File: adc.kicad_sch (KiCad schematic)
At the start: 37 parts, among them J5 Conn_01x03_Pin, J8 Conn_01x03_Pin, U21 LTC2299xUP

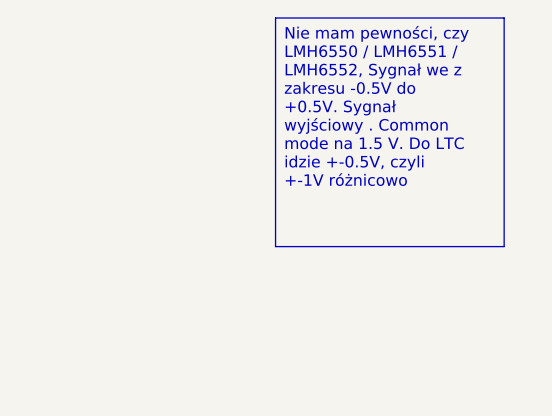
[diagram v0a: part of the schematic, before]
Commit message: Remove the stage between DAC and FET buffer
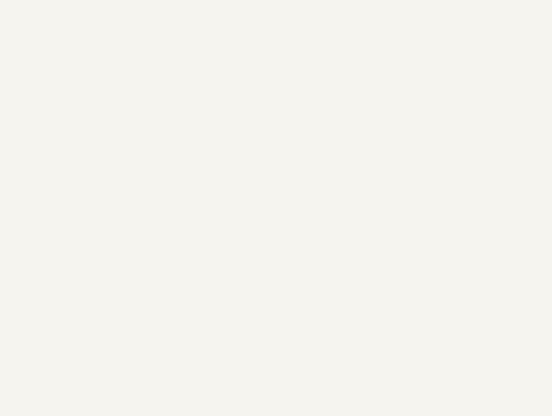
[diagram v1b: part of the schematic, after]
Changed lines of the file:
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@@
-		)
-	)
-	(text_box "Nie mam pewności, czy LMH6550 / LMH6551 / LMH6552, Sygnał we z zakresu -0.5V do +0.5V. Sygnał wyjściowy . Common mode na 1.5 V. Do LTC idzie +-0.5V, czyli +-1V różnicowo"
-		(exclude_from_sim no)
-		(at 372.11 24.13 0)
-		(size 25.4 25.4)
-		(margins 0.9525 0.9525 0.9525 0.9525)
-		(stroke
-			(width 0)
-			(type solid)
-		)
-		(fill
-			(type none)
-		)
-		(effects
-			(font
-				(size 1.27 1.27)
-			)
-			(justify left top)
 		)
 	)

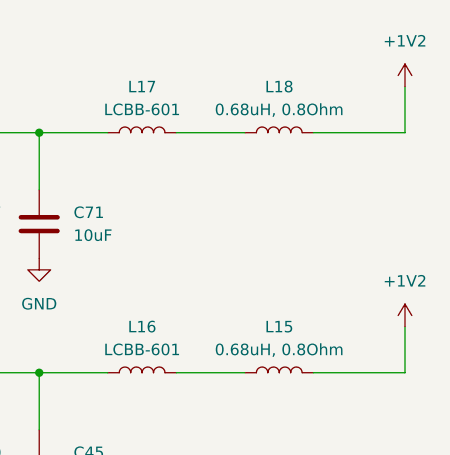
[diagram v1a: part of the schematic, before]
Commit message: Finished up schematic? - Added missing PSU lines
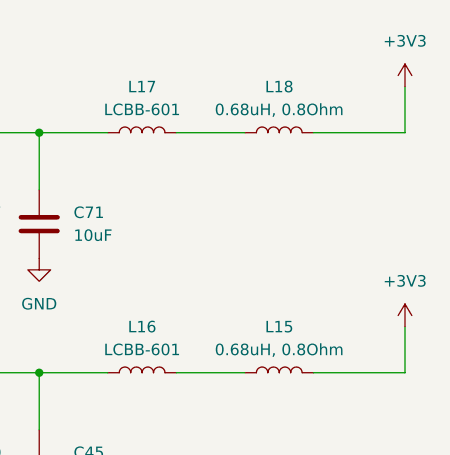
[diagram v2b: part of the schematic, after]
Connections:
- net +1V2 is gone; now on net +3V3: L15.1, L18.1
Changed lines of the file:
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@@
 	(wire
 		(pts
+			(xy 312.42 83.82) (xy 312.42 78.74)
+		)
+		(stroke
+			(width 0)
+			(type default)
+		)
+	)
+	(wire
+		(pts
 			(xy 237.49 57.15) (xy 237.49 130.81)
 		)
@@
 	(wire
 		(pts
-			(xy 312.42 83.82) (xy 312.42 78.74)
-		)
-		(stroke
-			(width 0)
-			(type default)
-		)
-	)
-	(wire
-		(pts
 			(xy 232.41 227.33) (xy 232.41 231.14)
 		)
@@
 	)
 	(symbol
-		(lib_id "power:+3V3")
-		(at 312.42 78.74 0)
-		(unit 1)
-		(exclude_from_sim no)
-		(in_bom yes)
-		(on_board yes)
-		(dnp no)
-		(fields_autoplaced yes)
-		(property "Reference" "#PWR0142"
-			(at 312.42 82.55 0)
-			(effects
-				(font
-					(size 1.27 1.27)
-				)
-				(hide yes)
-			)
-		)
-		(property "Value" "+1V2"
-			(at 312.42 73.66 0)
-			(effects
-				(font
-					(size 1.27 1.27)
-				)
-			)
-		)
-		(property "Footprint" ""
-			(at 312.42 78.74 0)
-			(effects
-				(font
-					(size 1.27 1.27)
-				)
-				(hide yes)
-			)
-		)
-		(property "Datasheet" ""
-			(at 312.42 78.74 0)
-			(effects
-				(font
-					(size 1.27 1.27)
-				)
-				(hide yes)
-			)
-		)
-		(property "Description" "Power symbol creates a global label with name \"+3V3\""
-			(at 312.42 78.74 0)
-			(effects
-				(font
-					(size 1.27 1.27)
-				)
-				(hide yes)
-			)
-		)
-		(pin "1"
-		)
-		(instances
-			(project "DigitalOsciloscope"
-				(path "/553deb7b-4100-40fe-99d2-0c7b4b56aad2/800cc051-5da0-4b0f-90b7-cfba3f489ea8"
-					(reference "#PWR0142")
-					(unit 1)
-				)
-			)
-		)
-	)
-	(symbol
 		(lib_id "Device:L")
 		(at 128.27 57.15 90)
@@
 	)
 	(symbol
-		(lib_id "power:+3V3")
-		(at 312.42 52.07 0)
-		(unit 1)
-		(exclude_from_sim no)
-		(in_bom yes)
-		(on_board yes)
-		(dnp no)
-		(fields_autoplaced yes)
-		(property "Reference" "#PWR0106"
-			(at 312.42 55.88 0)
-			(effects
-				(font
-					(size 1.27 1.27)
-				)
-				(hide yes)
-			)
-		)
-		(property "Value" "+1V2"
-			(at 312.42 46.99 0)
-			(effects
-				(font
-					(size 1.27 1.27)
-				)
-			)
-		)
-		(property "Footprint" ""
-			(at 312.42 52.07 0)
-			(effects
-				(font
-					(size 1.27 1.27)
-				)
-				(hide yes)
-			)
-		)
-		(property "Datasheet" ""
-			(at 312.42 52.07 0)
-			(effects
-				(font
-					(size 1.27 1.27)
-				)
-				(hide yes)
-			)
-		)
-		(property "Description" "Power symbol creates a global label with name \"+3V3\""
-			(at 312.42 52.07 0)
-			(effects
-				(font
-					(size 1.27 1.27)
-				)
-				(hide yes)
-			)
-		)
-		(pin "1"
-		)
-		(instances
-			(project "DigitalOsciloscope"
-				(path "/553deb7b-4100-40fe-99d2-0c7b4b56aad2/800cc051-5da0-4b0f-90b7-cfba3f489ea8"
-					(reference "#PWR0106")
-					(unit 1)
-				)
-			)
-		)
-	)
-	(symbol
 		(lib_id "Device:L")
 		(at 143.51 57.15 90)
@@
 	)
 	(symbol
+		(lib_id "power:+3V3")
+		(at 312.42 52.07 0)
+		(unit 1)
+		(exclude_from_sim no)
+		(in_bom yes)
+		(on_board yes)
+		(dnp no)
+		(fields_autoplaced yes)
+		(property "Reference" "#PWR0272"
+			(at 312.42 55.88 0)
+			(effects
+				(font
+					(size 1.27 1.27)
+				)
+				(hide yes)
+			)
+		)
+		(property "Value" "+3V3"
+			(at 312.42 46.99 0)
+			(effects
+				(font
+					(size 1.27 1.27)
+				)
+			)
+		)
+		(property "Footprint" ""
+			(at 312.42 52.07 0)
+			(effects
+				(font
+					(size 1.27 1.27)
+				)
+				(hide yes)
+			)
+		)
+		(property "Datasheet" ""
+			(at 312.42 52.07 0)
+			(effects
+				(font
+					(size 1.27 1.27)
+				)
+				(hide yes)
+			)
+		)
+		(property "Description" "Power symbol creates a global label with name \"+3V3\""
+			(at 312.42 52.07 0)
+			(effects
+				(font
+					(size 1.27 1.27)
+				)
+				(hide yes)
+			)
+		)
+		(pin "1"
+		)
+		(instances
+			(project "DigitalOsciloscope"
+				(path "/553deb7b-4100-40fe-99d2-0c7b4b56aad2/800cc051-5da0-4b0f-90b7-cfba3f489ea8"
+					(reference "#PWR0272")
+					(unit 1)
+				)
+			)
+		)
+	)
+	(symbol
 		(lib_id "Device:C")
 		(at 173.99 90.17 0)
@@
 					(unit 1)
 				)
+			)
+		)
+	)
+	(symbol
+		(lib_id "power:+3V3")
+		(at 312.42 78.74 0)
+		(unit 1)
+		(exclude_from_sim no)
+		(in_bom yes)
+		(on_board yes)
+		(dnp no)
+		(fields_autoplaced yes)
+		(property "Reference" "#PWR0106"
+			(at 312.42 82.55 0)
+			(effects
+				(font
+					(size 1.27 1.27)
+				)
+				(hide yes)
+			)
+		)
+		(property "Value" "+3V3"
+			(at 312.42 73.66 0)
+			(effects
+				(font
+					(size 1.27 1.27)
+				)
+			)
+		)
+		(property "Footprint" ""
+			(at 312.42 78.74 0)
+			(effects
+				(font
+					(size 1.27 1.27)
+				)
+				(hide yes)
+			)
+		)
+		(property "Datasheet" ""
+			(at 312.42 78.74 0)
+			(effects
+				(font
+					(size 1.27 1.27)
+				)
+				(hide yes)
+			)
+		)
+		(property "Description" "Power symbol creates a global label with name \"+3V3\""
+			(at 312.42 78.74 0)
+			(effects
+				(font
+					(size 1.27 1.27)
+				)
+				(hide yes)
+			)
+		)
+		(pin "1"
+		)
+		(instances
+			(project "DigitalOsciloscope"
+				(path "/553deb7b-4100-40fe-99d2-0c7b4b56aad2/800cc051-5da0-4b0f-90b7-cfba3f489ea8"
+					(reference "#PWR0106")
+					(unit 1)
+				)

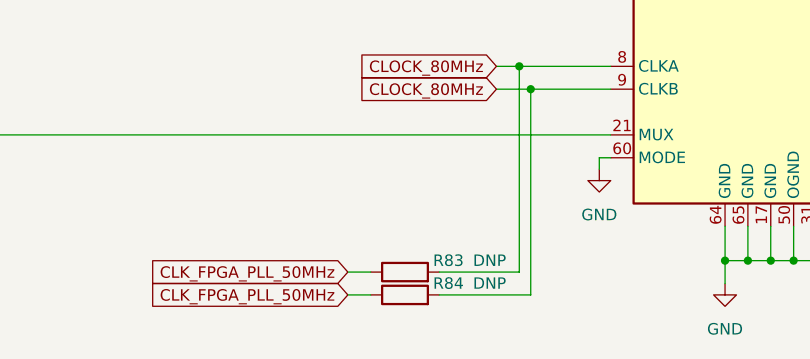
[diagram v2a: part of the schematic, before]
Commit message: Start working on ERC, properly annotate DNP elements
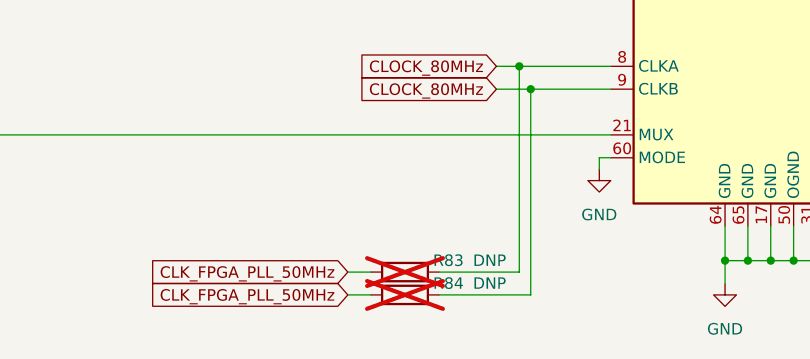
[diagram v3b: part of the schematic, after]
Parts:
- R83, R84: now not fitted
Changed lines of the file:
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@@
 		(in_bom yes)
 		(on_board yes)
-		(dnp no)
+		(dnp yes)
 		(property "Reference" "R84"
 			(at 196.596 233.68 90)
@@
 		(in_bom yes)
 		(on_board yes)
-		(dnp no)
+		(dnp yes)
 		(property "Reference" "R83"
 			(at 196.596 231.14 90)

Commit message: Fix ERC
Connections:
- net OVERFLOW: now reaches U21.57 (OFA)

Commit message: Add all footprints
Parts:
- J4: renamed from J8; footprint (none) -> TerminalBlock:TerminalBlock_MaiXu_MX126-5.0-03P_1x03_P5.00mm
- J5: footprint (none) -> TerminalBlock:TerminalBlock_MaiXu_MX126-5.0-03P_1x03_P5.00mm
- L33: renamed from L13; footprint (none) -> Inductor_SMD:L_0805_2012Metric
- L34: renamed from L7; footprint (none) -> Inductor_SMD:L_0805_2012Metric
- L35: renamed from L14; footprint (none) -> Inductor_SMD:L_0805_2012Metric
- L36: renamed from L8; footprint (none) -> Inductor_SMD:L_0805_2012Metric
- L37: renamed from L17; footprint (none) -> Inductor_SMD:L_0805_2012Metric
- L38: renamed from L16; footprint (none) -> Inductor_SMD:L_0805_2012Metric
- L39: renamed from L18; footprint (none) -> Inductor_SMD:L_0805_2012Metric
- L40: renamed from L15; footprint (none) -> Inductor_SMD:L_0805_2012Metric
- renumbered C39 to C76, C33 to C77, C40 to C78, C34 to C79, C41 to C80, C35 to C81, C16 to C82, C15 to C83, C42 to C84, C36 to C85, C18 to C86, C54 to C87, C43 to C88, C37 to C89, C17 to C90, C55 to C91, C44 to C92, C38 to C93, C46 to C94, C19 to C95, C47 to C96, C20 to C97, C71 to C98, C45 to C99, R83 to R56, R84 to R57, U21 to U9
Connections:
- net GND: no longer U9.11 (REFLB), U9.12 (REFLB), U9.13 (REFHB), U9.14 (REFHB)
- new net: U9.11 (REFLB), U9.12 (REFLB)
- new net: U9.13 (REFHB), U9.14 (REFHB)

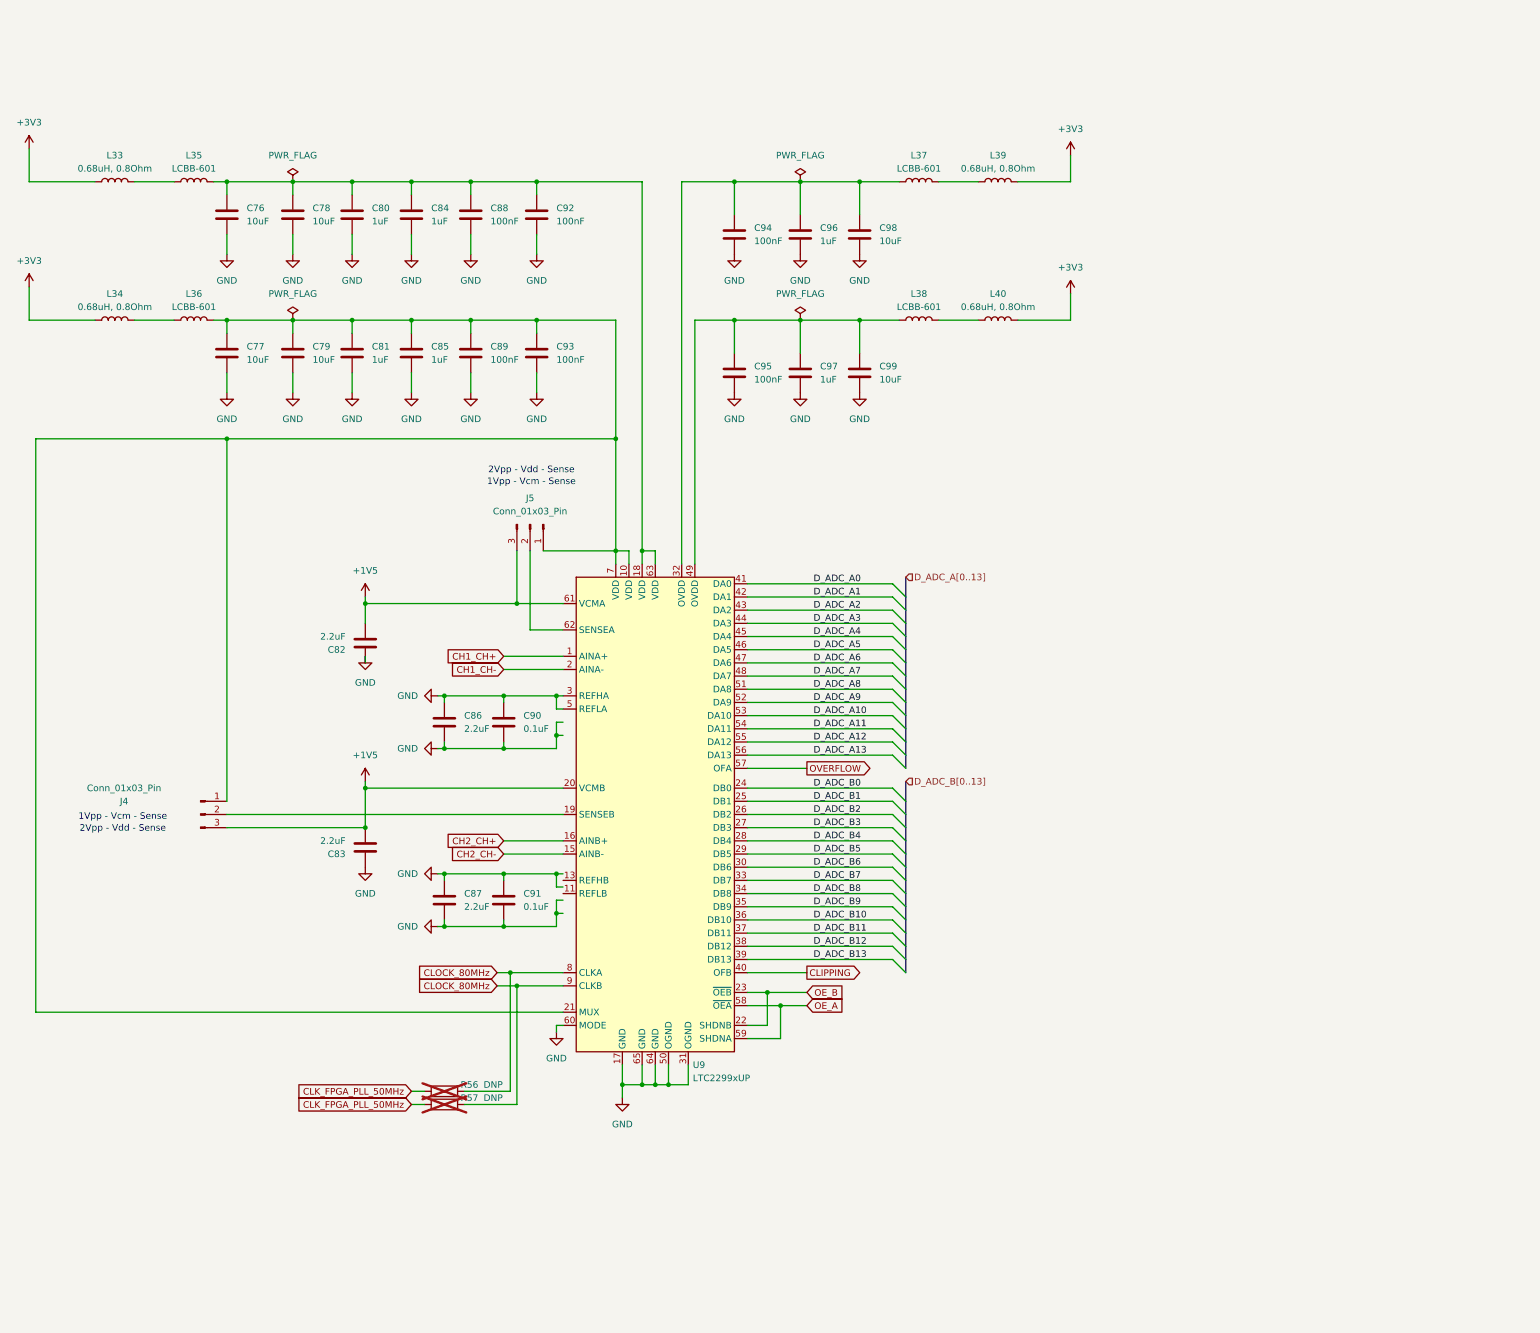
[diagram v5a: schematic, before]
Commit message: Apply changes after review, left to fix: comparator histeresis, PSU missing lines?
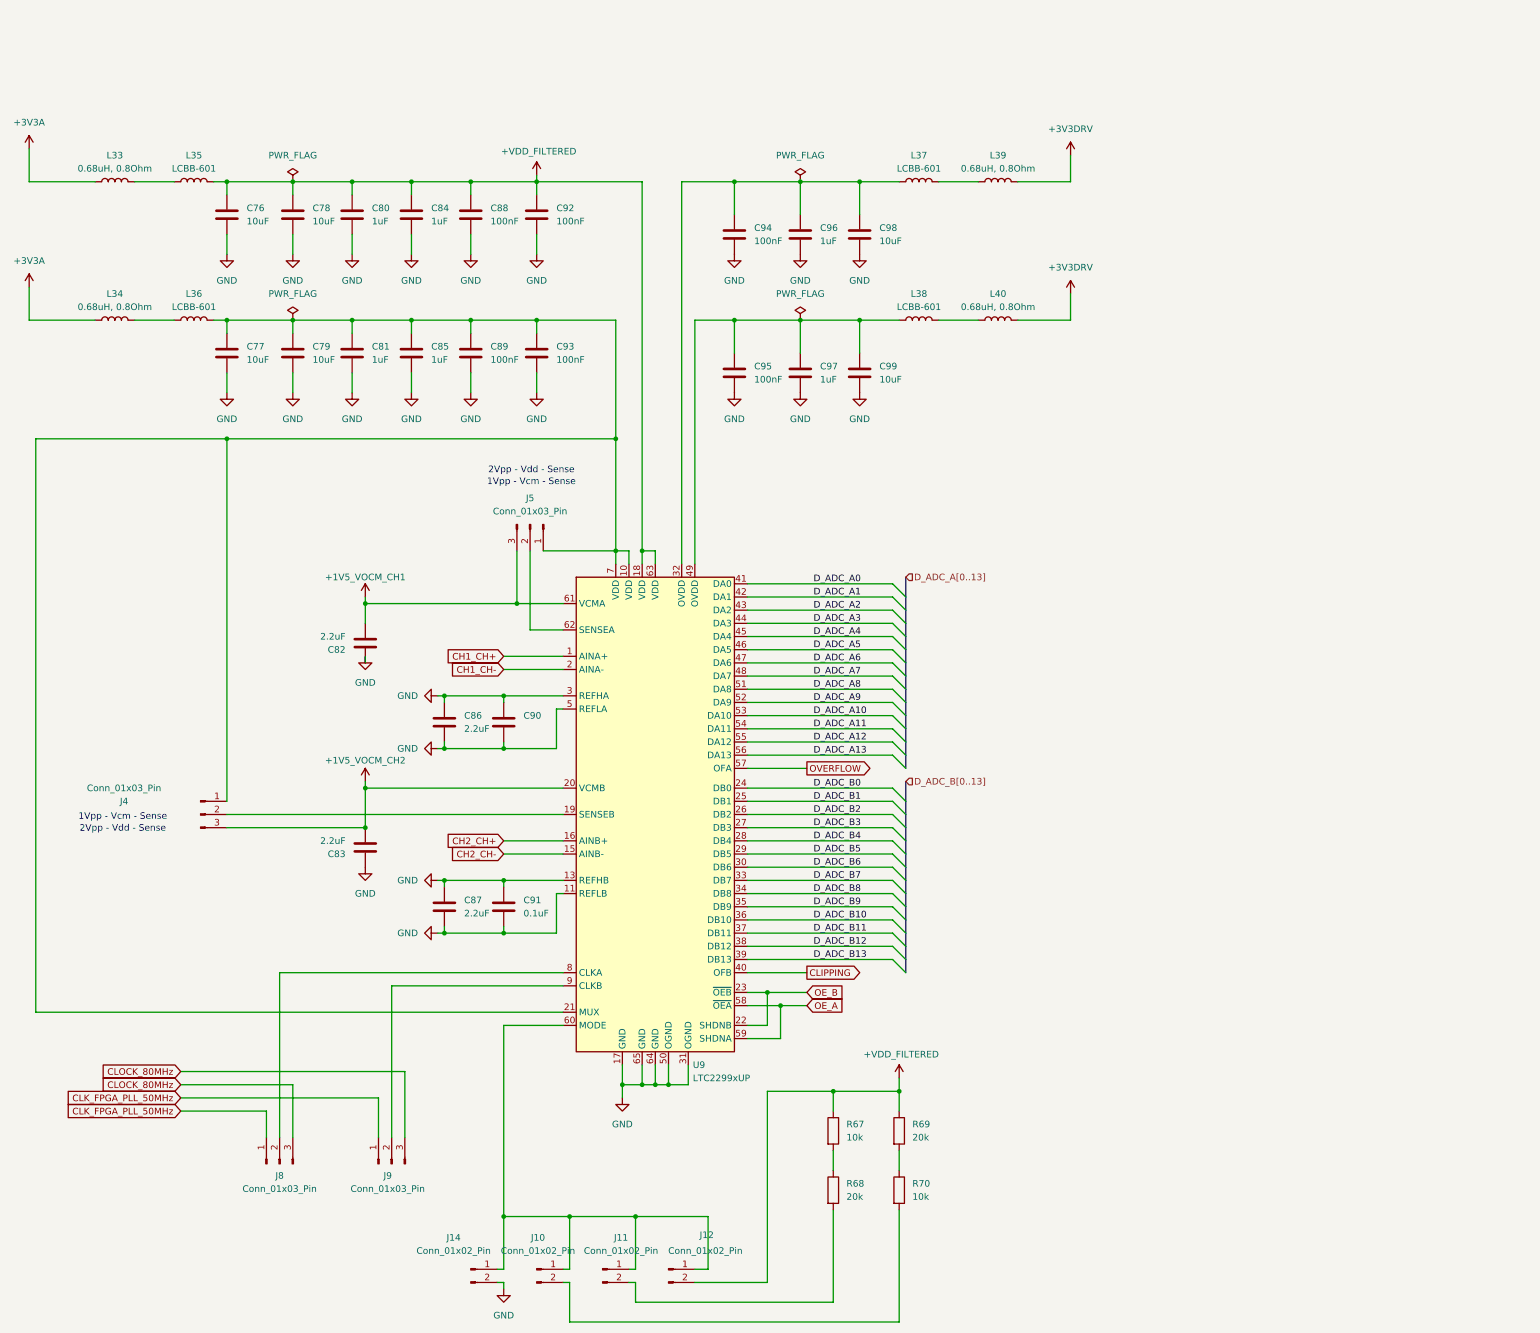
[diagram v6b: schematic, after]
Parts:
- removed R56, R57: DNP, Resistor_SMD:R_0805_2012Metric, symbol Device:R
- added J10, J11, J12, J14: Conn_01x02_Pin, TerminalBlock:TerminalBlock_MaiXu_MX126-5.0-02P_1x02_P5.00mm, symbol Connector:Conn_01x02_Pin
- added J8, J9: Conn_01x03_Pin, TerminalBlock:TerminalBlock_MaiXu_MX126-5.0-03P_1x03_P5.00mm, symbol Connector:Conn_01x03_Pin
- added R67, R70: 10k, Resistor_SMD:R_0805_2012Metric, symbol Device:R
- added R68, R69: 20k, Resistor_SMD:R_0805_2012Metric, symbol Device:R
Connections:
- net CLK_FPGA_PLL_50MHz: now also J8.1 (Pin_1), J9.1 (Pin_1)
- net CLOCK_80MHz: now also J8.3 (Pin_3), J9.3 (Pin_3); no longer U9.8 (CLKA), U9.9 (CLKB)
- net GND: now also U9.11 (REFLB), U9.12 (REFLB), U9.13 (REFHB), U9.14 (REFHB), J14.2 (Pin_2); no longer U9.60 (MODE)
- net +VDD_FILTERED: now reaches C76.1, C78.1, C80.1, C84.1, C88.1, C92.1, L35.2, U9.18 (VDD), U9.63 (VDD)
- net +VDD_FILTERED: now also J12.2 (Pin_2), R67.1, R69.1
- net +1V5 renamed +1V5_VOCM_CH1
- net +1V5_VOCM_CH1: no longer C83.1, J4.3 (Pin_3), U9.20 (VCMB)
- net +3V3 renamed +3V3A
- net +3V3A: no longer L39.1, L40.1
- new net: R69.2, R70.1
- new net: J10.2 (Pin_2), R70.2
- new net: J10.1 (Pin_1), J11.1 (Pin_1), J12.1 (Pin_1), J14.1 (Pin_1), U9.60 (MODE)
- new net: J8.2 (Pin_2), U9.8 (CLKA)
- new net: J11.2 (Pin_2), R68.2
- new net: R67.2, R68.1
- new net: J9.2 (Pin_2), U9.9 (CLKB)
- new net +1V5_VOCM_CH2: C83.1, J4.3 (Pin_3), U9.20 (VCMB)
- new net +3V3DRV: L39.1, L40.1
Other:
- moved on the sheet: C87, C91

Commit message: Save work before trying to add differential traces
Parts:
- J10, J11, J12, J14: footprint TerminalBlock:TerminalBlock_MaiXu_MX126-5.0-02P_1x02_P5.00mm -> Connector_PinHeader_2.54mm:PinHeader_1x02_P2.54mm_Vertical
- J8, J9: footprint TerminalBlock:TerminalBlock_MaiXu_MX126-5.0-03P_1x03_P5.00mm -> Connector_PinHeader_2.54mm:PinHeader_1x03_P2.54mm_Vertical
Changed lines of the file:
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@@
 			)
 		)
-		(property "Footprint" "TerminalBlock:TerminalBlock_MaiXu_MX126-5.0-02P_1x02_P5.00mm"
+		(property "Footprint" "Connector_PinHeader_2.54mm:PinHeader_1x02_P2.54mm_Vertical"
 			(at 196.85 266.7 0)
 			(effects
@@
 			)
 		)
-		(property "Footprint" "TerminalBlock:TerminalBlock_MaiXu_MX126-5.0-02P_1x02_P5.00mm"
+		(property "Footprint" "Connector_PinHeader_2.54mm:PinHeader_1x02_P2.54mm_Vertical"
 			(at 209.55 266.7 0)
 			(effects
@@
 			)
 		)
-		(property "Footprint" "TerminalBlock:TerminalBlock_MaiXu_MX126-5.0-03P_1x03_P5.00mm"
+		(property "Footprint" "Connector_PinHeader_2.54mm:PinHeader_1x03_P2.54mm_Vertical"
 			(at 160.02 246.38 0)
 			(effects
@@
 			)
 		)
-		(property "Footprint" "TerminalBlock:TerminalBlock_MaiXu_MX126-5.0-02P_1x02_P5.00mm"
+		(property "Footprint" "Connector_PinHeader_2.54mm:PinHeader_1x02_P2.54mm_Vertical"
 			(at 222.25 266.7 0)
 			(effects
@@
 			)
 		)
-		(property "Footprint" "TerminalBlock:TerminalBlock_MaiXu_MX126-5.0-02P_1x02_P5.00mm"
+		(property "Footprint" "Connector_PinHeader_2.54mm:PinHeader_1x02_P2.54mm_Vertical"
 			(at 234.95 266.7 0)
 			(effects
@@
 			)
 		)
-		(property "Footprint" "TerminalBlock:TerminalBlock_MaiXu_MX126-5.0-03P_1x03_P5.00mm"
+		(property "Footprint" "Connector_PinHeader_2.54mm:PinHeader_1x03_P2.54mm_Vertical"
 			(at 181.61 246.38 0)
 			(effects

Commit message: Save work before adding symetrical op amp
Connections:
- net CH1_CH+ renamed CH1_CH_P
- net CH1_CH- renamed CH1_CH_N
- net CH2_CH+ renamed CH2_CH_P
- net CH2_CH- renamed CH2_CH_N
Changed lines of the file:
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@@
 		)
 	)
-	(global_label "CH2_CH-"
+	(global_label "CH2_CH_N"
 		(shape input)
 		(at 203.2 186.69 180)
@@
 		)
 		(property "Intersheetrefs" "${INTERSHEET_REFS}"
-			(at 191.2643 186.69 0)
+			(at 190.5386 186.69 0)
 			(effects
 				(font
@@
 		)
 	)
-	(global_label "CH1_CH+"
+	(global_label "CH1_CH_P"
 		(shape input)
 		(at 203.2 148.59 180)
@@
 		)
 		(property "Intersheetrefs" "${INTERSHEET_REFS}"
-			(at 191.2643 148.59 0)
+			(at 190.5991 148.59 0)
 			(effects
 				(font
@@
 		)
 	)
-	(global_label "CH1_CH-"
+	(global_label "CH1_CH_N"
 		(shape input)
 		(at 203.2 151.13 180)
@@
 		)
 		(property "Intersheetrefs" "${INTERSHEET_REFS}"
-			(at 191.2643 151.13 0)
+			(at 190.5386 151.13 0)
 			(effects
 				(font
@@
 		)
 	)
-	(global_label "CH2_CH+"
+	(global_label "CH2_CH_P"
 		(shape input)
 		(at 203.2 184.15 180)
@@
 		)
 		(property "Intersheetrefs" "${INTERSHEET_REFS}"
-			(at 191.2643 184.15 0)
+			(at 190.5991 184.15 0)
 			(effects
 				(font
